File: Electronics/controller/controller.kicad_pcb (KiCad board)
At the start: 2 copper layers, 125.7 x 77.5 mm, 13 parts, among them P1 PROMICRO_A, P2 PROMICRO_B, P3 PANEL_2, P4 PANEL_1, P5 DIAL, P6 POWER, Q1 BS107, U1 LM317T

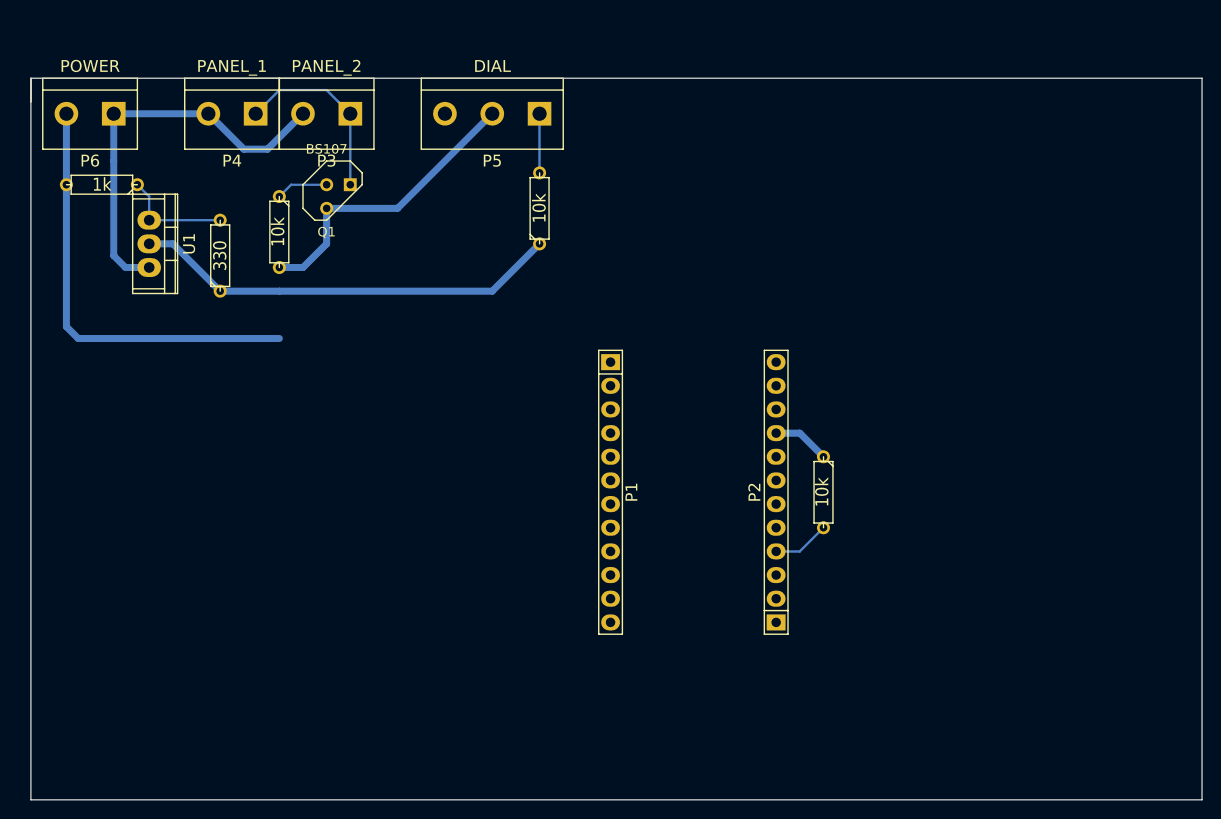
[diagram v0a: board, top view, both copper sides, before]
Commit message: Updated board layout. Tidied up schematic.
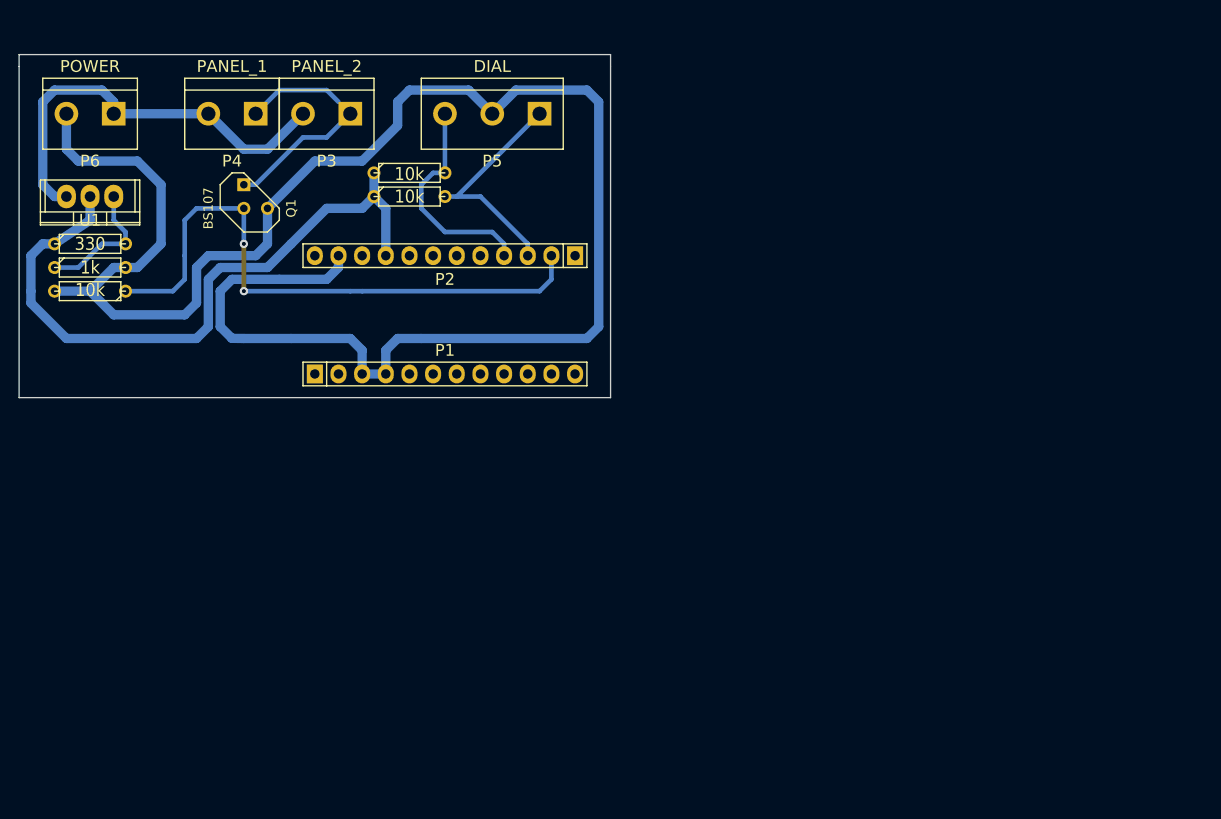
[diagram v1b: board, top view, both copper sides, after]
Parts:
- moved R3 56.1 mm to (143.5, 68.6), turned to 0 degrees
- moved P2 43.7 mm to (147.3, 77.5), turned to 180 degrees
- moved P1 21.8 mm to (147.3, 90.2), turned to 0 degrees
- moved R1 21.3 mm to (109.2, 81.3), turned to 180 degrees
- moved R2 14.0 mm to (143.5, 71.1), turned to 0 degrees
- moved R5 14.0 mm to (109.2, 76.2), turned to 0 degrees
- moved R4 8.98 mm to (109.2, 78.7), turned to 0 degrees
- moved Q1 8.89 mm to (127.0, 71.1), turned to 90 degrees
- moved U1 8.13 mm to (109.2, 71.1), turned to 180 degrees
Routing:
- net GND: track 78.2 -> 200.5 mm
- net /D16: track 5.61 -> 65.1 mm, vias 0 -> 2
- net +5V: track 52.3 -> 72.4 mm
- net /D14: track 6.35 -> 24.8 mm
- net /D15: track 6.13 -> 23.7 mm
- net Net-(P3-Pad1): track 19.9 -> 26.9 mm
- net +12V: track 43.1 -> 45.4 mm
- net Net-(R4-Pad1): track 12.0 -> 14.3 mm
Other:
- board size 125.7 x 77.5 mm -> 63.5 x 36.8 mm
- net class Default: trace_width 0.254 -> 0.5
- net class Power: trace_width 0.75 -> 1

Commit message: Add display driver schematic.
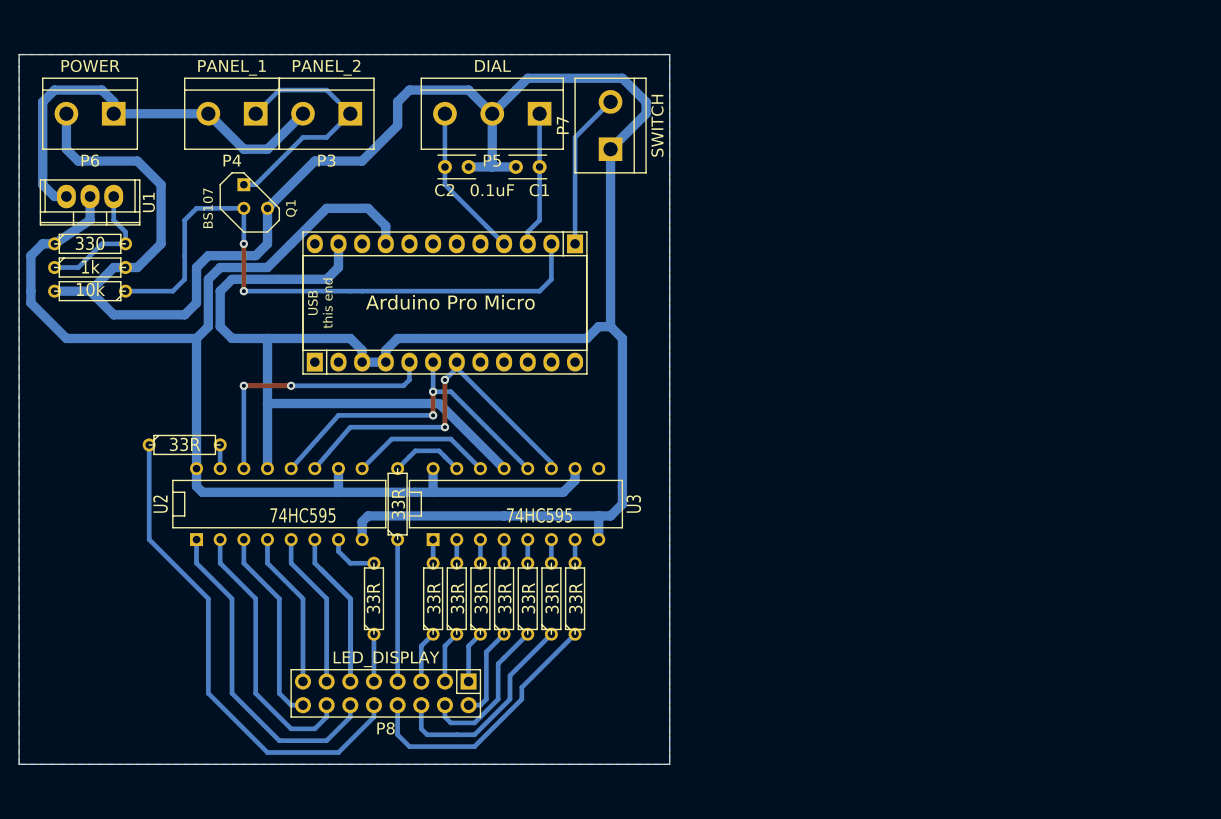
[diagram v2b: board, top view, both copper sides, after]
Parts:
- added C1: 0.1uF, Capacitors_ThroughHole:Capacitor4x3RM2.5, F.Cu at (157.5, 67.9)
- added C2: 0.1uF, Capacitors_ThroughHole:Capacitor4x3RM2.5, F.Cu at (149.9, 67.9)
- added P7: SWITCH, Connect:bornier2, F.Cu at (165.1, 63.5)
- added P8: LED_DISPLAY, Pin_Headers:Pin_Header_Straight_2x08, F.Cu at (141.0, 124.5)
- added R10: 33R, Discret:R3, F.Cu at (146.1, 114.3)
- added R11: 33R, Discret:R3, F.Cu at (151.1, 114.3)
- added R12: 33R, Discret:R3, F.Cu at (156.2, 114.3)
- added R13: 33R, Discret:R3, F.Cu at (161.3, 114.3)
- added R6: 33R, Discret:R3, F.Cu at (142.2, 104.1)
- added R7: 33R, Discret:R3, F.Cu at (148.6, 114.3)
- added R8: 33R, Discret:R3, F.Cu at (153.7, 114.3)
- added R9: 33R, Discret:R3, F.Cu at (158.8, 114.3)
- added U2: 74HC595, Sockets_DIP:DIP-16__300, F.Cu at (129.5, 104.1)
- added U3: 74HC595, Sockets_DIP:DIP-16__300, F.Cu at (154.9, 104.1)
- R2, R3: value 10k -> 33R
- moved R3 45.9 mm to (139.7, 114.3), turned to 90 degrees
- moved R2 36.0 mm to (119.4, 97.8)
- moved P1 1.27 mm to (147.3, 88.9)
- moved P2 1.27 mm to (147.3, 76.2)
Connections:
- R2 pad 1: +5V -> /LED_P
- R2 pad 2: /D14 -> Net-(R2-Pad2)
- R3 pad 1: +5V -> /LED_P_AN
- R3 pad 2: /D15 -> Net-(R3-Pad2)
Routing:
- net GND: track 200.5 -> 314.0 mm
- net +5V: track 72.4 -> 130.1 mm
- net /LED_P: track 0.00 -> 52.6 mm
- net /D4: track 0.00 -> 39.2 mm, vias 0 -> 2
- net /D3: track 0.00 -> 37.1 mm, vias 0 -> 2
- net /LED_CN_AN: track 0.00 -> 35.2 mm
- net /LED_F: track 0.00 -> 30.2 mm
- net /LED_A: track 0.00 -> 29.7 mm
- net /D2: track 0.00 -> 28.8 mm, vias 0 -> 2
- net /LED_D4: track 0.00 -> 28.5 mm
- net /LED_D3: track 0.00 -> 22.7 mm
- net /LED_B: track 0.00 -> 21.8 mm
- net /D10: track 0.00 -> 16.8 mm
- net /LED_G: track 0.00 -> 16.8 mm
- net /LED_C: track 0.00 -> 16.8 mm
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- added copper zone on B.Cu, net GND
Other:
- board size 63.5 x 36.8 mm -> 69.8 x 76.2 mm
- board text added: "Arduino Pro Micro"
- board text added: "USB this end"

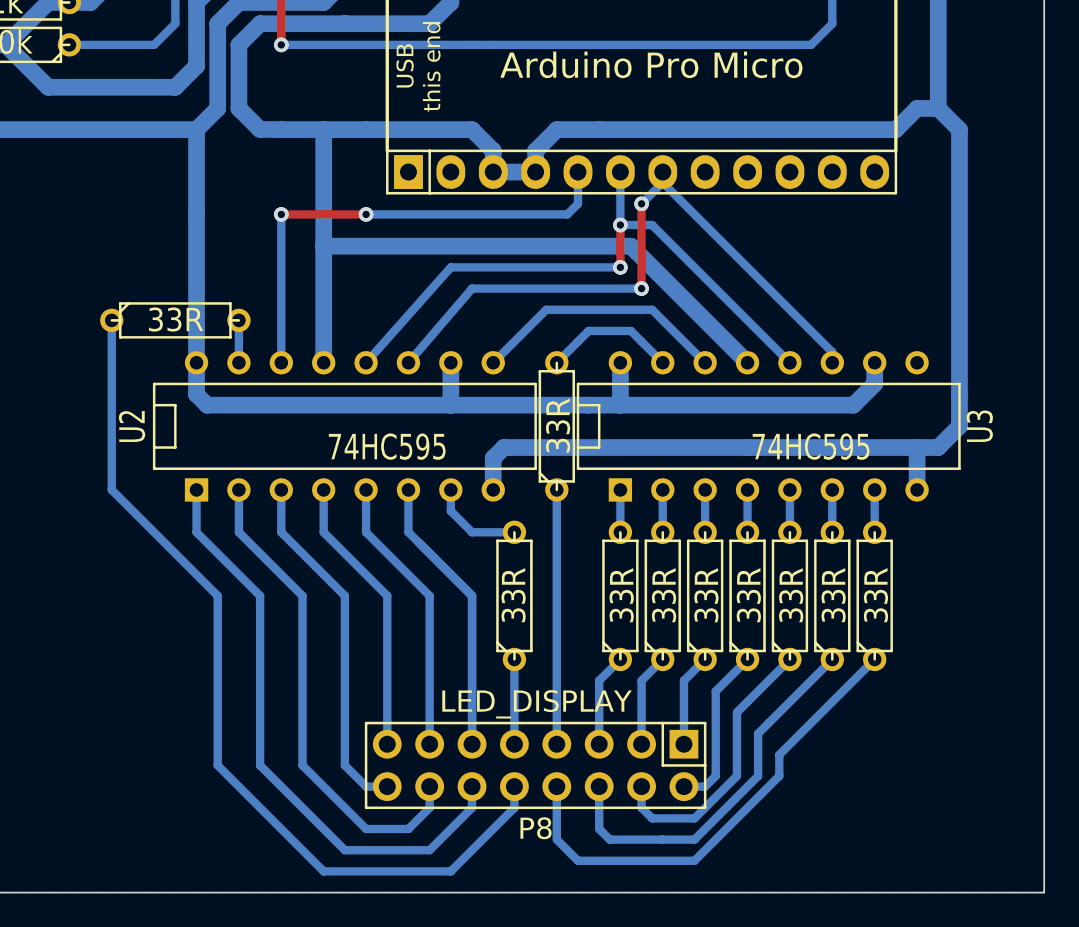
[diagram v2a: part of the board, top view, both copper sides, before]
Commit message: Update schematics with new single-SIPO implementation.
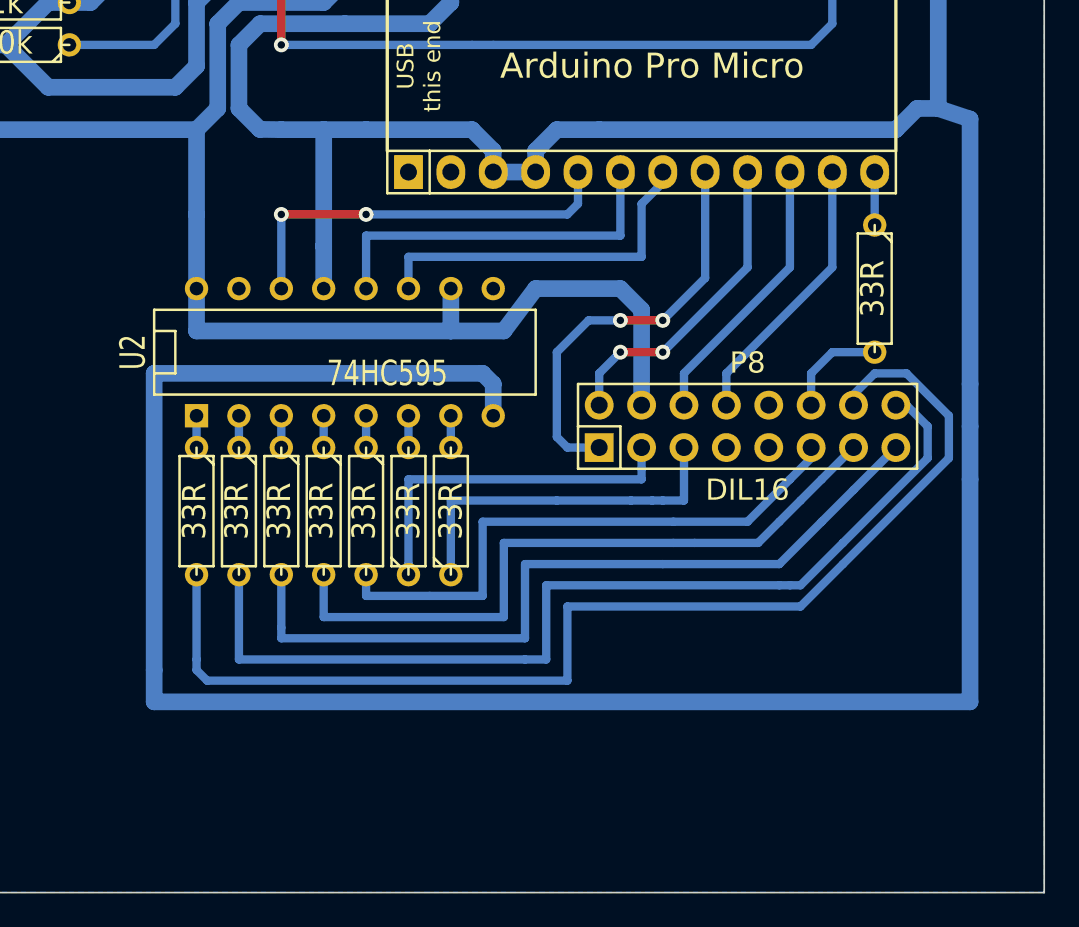
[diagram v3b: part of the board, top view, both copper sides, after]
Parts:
- removed R12, R13: 33R, Discret:R3
- removed U3: 74HC595, Sockets_DIP:DIP-16__300
- P8: value LED_DISPLAY -> DIL16
- moved R8 33.4 mm to (120.7, 109.2), turned to 270 degrees
- moved R9 30.9 mm to (128.3, 109.2), turned to 270 degrees
- moved P8 24.0 mm to (153.7, 104.1), turned to 0 degrees
- moved R10 23.9 mm to (161.3, 95.9), turned to 270 degrees
- moved R7 23.4 mm to (125.7, 109.2), turned to 270 degrees
- moved R11 20.9 mm to (130.8, 109.2), turned to 270 degrees
- moved R6 19.7 mm to (123.2, 109.2), turned to 270 degrees
- moved R2 18.1 mm to (133.3, 109.2), turned to 90 degrees
- moved R3 6.35 mm to (135.9, 109.2)
- moved U2 4.45 mm to (129.5, 99.7)
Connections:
- net Net-(R3-Pad2) renamed /E
- P8 pad 1: /LED_D1 -> /D5
- P8 pad 10: /LED_P -> Net-(P8-Pad10)
- P8 pad 11: /LED_F -> Net-(P8-Pad11)
- P8 pad 12: /LED_CN_AN -> Net-(P8-Pad12)
- P8 pad 13: /LED_C -> Net-(P8-Pad13)
- P8 pad 14: /LED_A -> Net-(P8-Pad14)
- P8 pad 15: /LED_G -> Net-(P8-Pad15)
- P8 pad 16: /LED_B -> Net-(P8-Pad16)
- P8 pad 2: /LED_D2 -> /D6
- P8 pad 3: /LED_D -> Net-(P8-Pad3)
- P8 pad 4: /LED_CN -> +5V
- P8 pad 5: /LED_E -> Net-(P8-Pad5)
- P8 pad 6: /LED_D3 -> /D7
- P8 pad 7: /LED_DP -> Net-(P8-Pad7)
- P8 pad 8: /LED_D4 -> /D8
- P8 pad 9: /LED_P_AN -> Net-(P8-Pad9)
- R10 pad 1: /LED_E -> /D9
- R10 pad 2: Net-(R10-Pad2) -> Net-(P8-Pad12)
- R11 pad 1: /LED_D1 -> /F
- R11 pad 2: Net-(R11-Pad2) -> Net-(P8-Pad11)
- R2 pad 1: /LED_P -> Net-(P8-Pad3)
- R2 pad 2: Net-(R2-Pad2) -> /D
- R3 pad 1: /LED_P_AN -> Net-(P8-Pad5)
- R6 pad 1: /LED_DP -> /B
- R6 pad 2: Net-(R6-Pad2) -> Net-(P8-Pad16)
- R7 pad 1: /LED_D -> /G
- R7 pad 2: Net-(R7-Pad2) -> Net-(P8-Pad15)
- R8 pad 1: /LED_D2 -> /A
- R8 pad 2: Net-(R8-Pad2) -> Net-(P8-Pad14)
- R9 pad 1: /LED_D3 -> /C
- R9 pad 2: Net-(R9-Pad2) -> Net-(P8-Pad13)
- U2 pad 1: /LED_CN_AN -> /A
- U2 pad 15: Net-(R2-Pad2) -> Net-(U2-Pad15)
- U2 pad 2: /LED_A -> /B
- U2 pad 3: /LED_B -> /G
- U2 pad 4: /LED_G -> /C
- U2 pad 5: /LED_C -> /F
- U2 pad 6: /LED_F -> /D
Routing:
- net Net-(P8-Pad14): track 0.00 -> 69.7 mm
- net Net-(P8-Pad16): track 0.00 -> 58.3 mm
- net /LED_P: track 52.6 -> 0.00 mm
- net Net-(P8-Pad15): track 0.00 -> 48.0 mm
- net GND: track 314.0 -> 356.5 mm
- net Net-(P8-Pad13): track 0.00 -> 41.1 mm
- net /LED_CN_AN: track 35.2 -> 0.00 mm
- net Net-(P8-Pad11): track 0.00 -> 34.6 mm
- net /LED_F: track 30.2 -> 0.00 mm
- net /LED_A: track 29.7 -> 0.00 mm
- net /LED_D4: track 28.5 -> 0.00 mm
- net /D5: track 0.00 -> 25.0 mm, vias 0 -> 2
- net /LED_D3: track 22.7 -> 0.00 mm
- net /LED_B: track 21.8 -> 0.00 mm
- net Net-(P8-Pad5): track 0.00 -> 21.6 mm
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
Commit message: Fix layout.
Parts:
- removed P1: PROMICRO_A, Pin_Headers:Pin_Header_Straight_1x12
- removed P2: PROMICRO_B, Pin_Headers:Pin_Header_Straight_1x12
- added U3: Arduino_Pro_Micro, Cylindric:ArduinoProMicro, F.Cu at (138.4, 78.7)
- P8: value DIL16 -> LED_DISPLAY
- Q1: value BS107 -> BUZ11; footprint Discret:TO92 -> Transistors_TO-220:TO-220_FET-GDS_Vertical
- moved R1 55.8 mm to (162.6, 64.8), turned to 0 degrees
- moved R4 14.3 mm to (122.6, 73.7)
- moved R5 14.3 mm to (122.6, 71.1), turned to 180 degrees
- moved P6 8.52 mm to (116.8, 58.4)
- moved Q1 8.13 mm to (133.3, 66.0), turned to 0 degrees
- moved U1 6.25 mm to (114.9, 68.6), turned to 90 degrees
- moved C2 5.99 mm to (144.8, 64.8), turned to 0 degrees
- moved P4 5.39 mm to (128.3, 58.4)
- moved P3 5.39 mm to (138.4, 58.4)
- moved P7 5.24 mm to (166.4, 58.4), turned to 180 degrees
- moved P5 3.81 mm to (152.4, 58.4)
- moved C1 3.42 mm to (156.2, 64.8)
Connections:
- net +5V renamed VCC
- P6 pad 1: +12V -> GND
- P6 pad 2: GND -> +12V
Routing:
- net /D16: track 66.3 -> 36.8 mm, vias 2 -> 4
- net VCC: track 115.2 -> 93.2 mm
- net GND: track 356.5 -> 335.9 mm
- net +12V: track 45.4 -> 34.5 mm
- net Net-(R4-Pad1): track 14.3 -> 6.35 mm
- net Net-(P3-Pad1): track 26.9 -> 19.5 mm
- net /D10: track 16.8 -> 13.8 mm
- net /D14: track 14.5 -> 12.8 mm
- net /D15: track 16.6 -> 17.6 mm
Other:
- board outline removed
- board text removed: "Arduino Pro Micro"
- board text removed: "USB this end"
